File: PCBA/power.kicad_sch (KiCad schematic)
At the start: 8 parts, among them Q702 MMBT3904, U702 TC2014-3.3VxCTTR

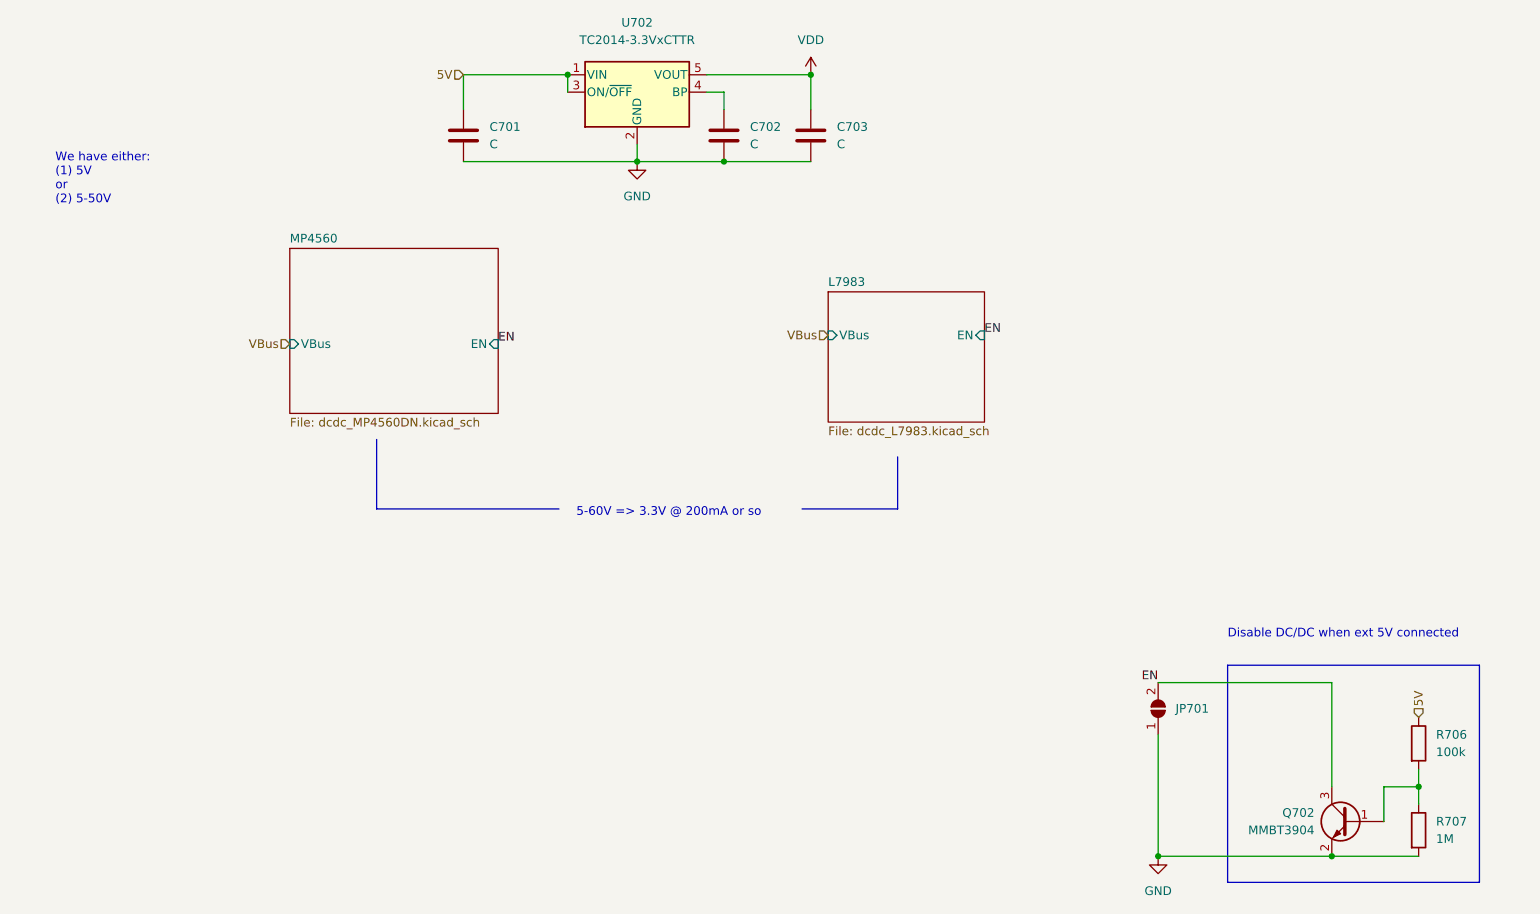
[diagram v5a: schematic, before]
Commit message: Step models for ports
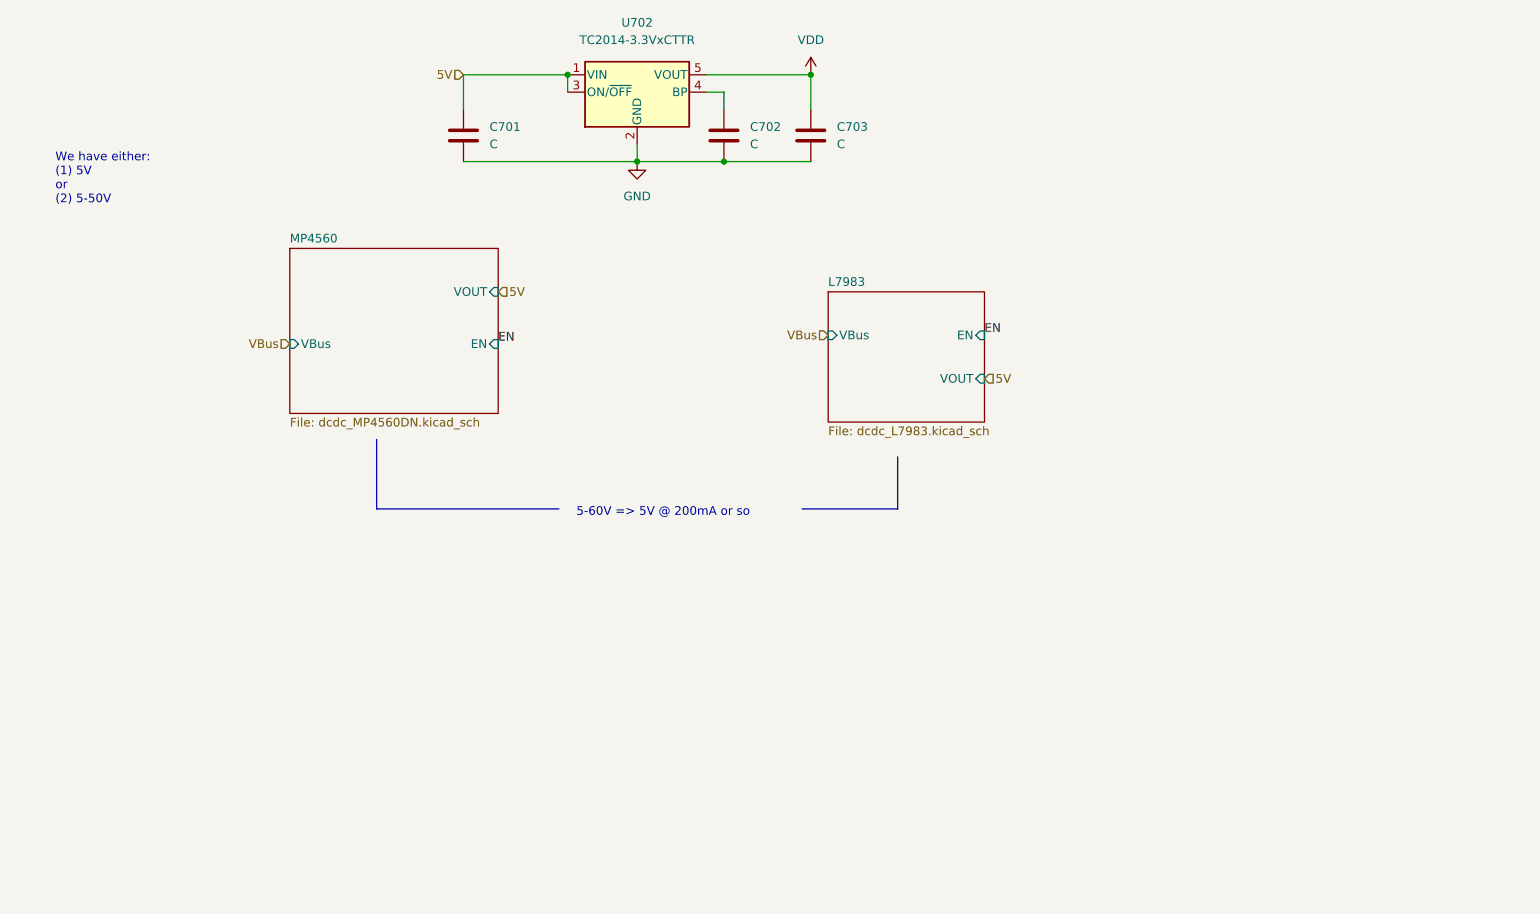
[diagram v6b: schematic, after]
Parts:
- removed JP701: Disable, Jumper:SolderJumper-2_P1.3mm_Open_Pad1.0x1.5mm, symbol Jumper:SolderJumper_2_Open
- removed Q702: MMBT3904, Package_TO_SOT_SMD:SOT-23, symbol Transistor_BJT:MMBT3904
- removed R706: 100k, Resistor_SMD:R_0603_1608Metric, symbol Device:R
- removed R707: 1M, Resistor_SMD:R_0603_1608Metric, symbol Device:R
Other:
- sheet L7983 ports: added VOUT; removed none
- sheet MP4560 ports: added VOUT; removed none
- note added: "5-60V => 5V @ 200mA or so"
- note removed: "5-60V => 3.3V @ 200mA or so"
- note removed: "Disable DC/DC when ext 5V connected"
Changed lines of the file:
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@@
 (kicad_sch (version 20211123) (generator eeschema)
   (paper "A4")
-  (junction (at 266.7 129.54) (diameter 0) (color 0 0 0 0)
-  )
-  (junction (at 228.6 139.7) (diameter 0) (color 0 0 0 0)
-  )
   (junction (at 142.24 25.4) (diameter 0) (color 0 0 0 0)
   )
   (junction (at 152.4 38.1) (diameter 0) (color 0 0 0 0)
   )
-  (junction (at 254 139.7) (diameter 0) (color 0 0 0 0)
-  )
   (junction (at 165.1 38.1) (diameter 0) (color 0 0 0 0)
   )
@@
     (stroke (width 0) (type default) (color 0 0 0 0))
   )
-  (wire (pts (xy 261.62 134.62) (xy 261.62 129.54))
-    (stroke (width 0) (type default) (color 0 0 0 0))
-  )
   (wire (pts (xy 165.1 27.94) (xy 165.1 30.48))
     (stroke (width 0) (type default) (color 0 0 0 0))
@@
     (stroke (width 0) (type default) (color 0 0 0 0))
   )
-  (polyline (pts (xy 238.76 111.76) (xy 275.59 111.76))
-    (stroke (width 0) (type default) (color 0 0 0 0))
-  )
-  (wire (pts (xy 266.7 127) (xy 266.7 129.54))
-    (stroke (width 0) (type default) (color 0 0 0 0))
-  )
   (wire (pts (xy 162.56 25.4) (xy 177.8 25.4))
     (stroke (width 0) (type default) (color 0 0 0 0))
   )
-  (wire (pts (xy 228.6 139.7) (xy 254 139.7))
-    (stroke (width 0) (type default) (color 0 0 0 0))
-  )
   (wire (pts (xy 162.56 27.94) (xy 165.1 27.94))
     (stroke (width 0) (type default) (color 0 0 0 0))
@@
     (stroke (width 0) (type default) (color 0 0 0 0))
   )
-  (wire (pts (xy 254 139.7) (xy 266.7 139.7))
-    (stroke (width 0) (type default) (color 0 0 0 0))
-  )
-  (wire (pts (xy 228.6 139.7) (xy 228.6 121.92))
-    (stroke (width 0) (type default) (color 0 0 0 0))
-  )
   (polyline (pts (xy 114.3 78.74) (xy 114.3 88.9))
     (stroke (width 0) (type default) (color 0 0 0 0))
   )
-  (polyline (pts (xy 275.59 143.51) (xy 275.59 111.76))
-    (stroke (width 0) (type default) (color 0 0 0 0))
-  )
   (polyline (pts (xy 190.5 81.28) (xy 190.5 88.9))
     (stroke (width 0) (type default) (color 0 0 0 0))
   )
-  (wire (pts (xy 254 114.3) (xy 254 129.54))
-    (stroke (width 0) (type default) (color 0 0 0 0))
-  )
   (wire (pts (xy 152.4 35.56) (xy 152.4 38.1))
     (stroke (width 0) (type default) (color 0 0 0 0))
   )
-  (wire (pts (xy 266.7 129.54) (xy 266.7 132.08))
-    (stroke (width 0) (type default) (color 0 0 0 0))
-  )
   (wire (pts (xy 177.8 25.4) (xy 177.8 30.48))
     (stroke (width 0) (type default) (color 0 0 0 0))
   )
-  (polyline (pts (xy 238.76 143.51) (xy 275.59 143.51))
-    (stroke (width 0) (type default) (color 0 0 0 0))
-  )
   (polyline (pts (xy 176.53 88.9) (xy 190.5 88.9))
     (stroke (width 0) (type default) (color 0 0 0 0))
@@
     (stroke (width 0) (type default) (color 0 0 0 0))
   )
-  (wire (pts (xy 228.6 114.3) (xy 254 114.3))
-    (stroke (width 0) (type default) (color 0 0 0 0))
-  )
   (wire (pts (xy 142.24 25.4) (xy 142.24 27.94))
     (stroke (width 0) (type default) (color 0 0 0 0))
   )
-  (polyline (pts (xy 238.76 111.76) (xy 238.76 143.51))
-    (stroke (width 0) (type default) (color 0 0 0 0))
-  )
-  (wire (pts (xy 261.62 129.54) (xy 266.7 129.54))
-    (stroke (width 0) (type default) (color 0 0 0 0))
-  )
   (wire (pts (xy 165.1 38.1) (xy 177.8 38.1))
     (stroke (width 0) (type default) (color 0 0 0 0))
   )
-  (text "Disable DC/DC when ext 5V connected" (at 238.76 107.95 0)
-    (effects (font (size 1.27 1.27)) (justify left bottom))
-  )
   (text "We have either:\n(1) 5V\nor\n(2) 5-50V" (at 67.31 44.45 0)
     (effects (font (size 1.27 1.27)) (justify left bottom))
   )
-  (text "5-60V => 3.3V @ 200mA or so" (at 143.51 90.17 0)
+  (text "5-60V => 5V @ 200mA or so" (at 143.51 90.17 0)
     (effects (font (size 1.27 1.27)) (justify left bottom))
   )
@@
   (label "EN" (at 203.2 63.5 0)
     (effects (font (size 1.27 1.27)) (justify left bottom))
-  )
-  (label "EN" (at 228.6 114.3 180)
-    (effects (font (size 1.27 1.27)) (justify right bottom))
   )
   (hierarchical_label "VBus" (shape input) (at 101.6 64.77 180)
     (effects (font (size 1.27 1.27)) (justify right))
   )
-  (hierarchical_label "5V" (shape input) (at 266.7 119.38 90)
+  (hierarchical_label "5V" (shape input) (at 203.2 69.85 0)
+    (effects (font (size 1.27 1.27)) (justify left))
+  )
+  (hierarchical_label "5V" (shape input) (at 132.08 57.15 0)
     (effects (font (size 1.27 1.27)) (justify left))
   )
@@
     (pin "5")
   )
-  (symbol (lib_id "Jumper:SolderJumper_2_Open") (at 228.6 118.11 90) (unit 1)
-    (in_bom yes) (on_board yes) (fields_autoplaced)
-    (property "Reference" "JP701" (id 0) (at 231.14 118.1099 90)
-      (effects (font (size 1.27 1.27)) (justify right))
-    )
-    (property "Value" "Disable" (id 1) (at 231.14 119.3799 90)
-      (effects (font (size 1.27 1.27)) (justify right) hide)
-    )
-    (property "Footprint" "Jumper:SolderJumper-2_P1.3mm_Open_Pad1.0x1.5mm" (id 2) (at 228.6 118.11 0)
-      (effects (font (size 1.27 1.27)) hide)
-    )
-    (property "Datasheet" "~" (id 3) (at 228.6 118.11 0)
-      (effects (font (size 1.27 1.27)) hide)
-    )
-    (pin "1")
-    (pin "2")
-  )
   (symbol (lib_id "Device:C") (at 165.1 34.29 0) (unit 1)
     (in_bom yes) (on_board yes) (fields_autoplaced)
@@
     (pin "2")
   )
-  (symbol (lib_id "Device:R") (at 266.7 123.19 0) (unit 1)
-    (in_bom yes) (on_board yes) (fields_autoplaced)
-    (property "Reference" "R706" (id 0) (at 269.24 121.9199 0)
-      (effects (font (size 1.27 1.27)) (justify left))
-    )
-    (property "Value" "100k" (id 1) (at 269.24 124.4599 0)
-      (effects (font (size 1.27 1.27)) (justify left))
-    )
-    (property "Footprint" "Resistor_SMD:R_0603_1608Metric" (id 2) (at 264.922 123.19 90)
-      (effects (font (size 1.27 1.27)) hide)
-    )
-    (property "Datasheet" "~" (id 3) (at 266.7 123.19 0)
-      (effects (font (size 1.27 1.27)) hide)
-    )
-    (pin "1")
-    (pin "2")
-  )
-  (symbol (lib_id "Device:R") (at 266.7 135.89 0) (unit 1)
-    (in_bom yes) (on_board yes) (fields_autoplaced)
-    (property "Reference" "R707" (id 0) (at 269.24 134.6199 0)
-      (effects (font (size 1.27 1.27)) (justify left))
-    )
-    (property "Value" "1M" (id 1) (at 269.24 137.1599 0)
-      (effects (font (size 1.27 1.27)) (justify left))
-    )
-    (property "Footprint" "Resistor_SMD:R_0603_1608Metric" (id 2) (at 264.922 135.89 90)
-      (effects (font (size 1.27 1.27)) hide)
-    )
-    (property "Datasheet" "~" (id 3) (at 266.7 135.89 0)
-      (effects (font (size 1.27 1.27)) hide)
-    )
-    (pin "1")
-    (pin "2")
-  )
   (symbol (lib_id "Device:C") (at 177.8 34.29 0) (unit 1)
     (in_bom yes) (on_board yes) (fields_autoplaced)
@@
     (pin "2")
   )
-  (symbol (lib_id "power:GND") (at 228.6 139.7 0) (unit 1)
-    (in_bom yes) (on_board yes) (fields_autoplaced)
-    (property "Reference" "#PWR0154" (id 0) (at 228.6 146.05 0)
-      (effects (font (size 1.27 1.27)) hide)
-    )
-    (property "Value" "GND" (id 1) (at 228.6 144.78 0))
-    (property "Footprint" "" (id 2) (at 228.6 139.7 0)
-      (effects (font (size 1.27 1.27)) hide)
-    )
-    (property "Datasheet" "" (id 3) (at 228.6 139.7 0)
-      (effects (font (size 1.27 1.27)) hide)
-    )
-    (pin "1")
-  )
   (symbol (lib_id "Device:C") (at 127 34.29 0) (unit 1)
     (in_bom yes) (on_board yes) (fields_autoplaced)
@@
     (pin "1")
     (pin "2")
-  )
-  (symbol (lib_id "Transistor_BJT:MMBT3904") (at 256.54 134.62 0) (mirror y) (unit 1)
-    (in_bom yes) (on_board yes) (fields_autoplaced)
-    (property "Reference" "Q702" (id 0) (at 251.46 133.3499 0)
-      (effects (font (size 1.27 1.27)) (justify left))
-    )
-    (property "Value" "MMBT3904" (id 1) (at 251.46 135.8899 0)
-      (effects (font (size 1.27 1.27)) (justify left))
-    )
-    (property "Footprint" "Package_TO_SOT_SMD:SOT-23" (id 2) (at 251.46 136.525 0)
-      (effects (font (size 1.27 1.27) italic) (justify left) hide)
-    )
-    (property "Datasheet" "https://www.onsemi.com/pub/Collateral/2N3903-D.PDF" (id 3) (at 256.54 134.62 0)
-      (effects (font (size 1.27 1.27)) (justify left) hide)
-    )
-    (pin "1")
-    (pin "2")
-    (pin "3")
   )
   (symbol (lib_id "power:VDD") (at 177.8 25.4 0) (unit 1)
@@
       (effects (font (size 1.27 1.27)) (justify right))
     )
+    (pin "VOUT" input (at 203.2 69.85 0)
+      (effects (font (size 1.27 1.27)) (justify right))
+    )
   )
   (sheet (at 101.6 50.8) (size 30.48 24.13) (fields_autoplaced)
@@
       (effects (font (size 1.27 1.27)) (justify left))
     )
-  )
+    (pin "VOUT" input (at 132.08 57.15 0)
+      (effects (font (size 1.27 1.27)) (justify right))
+    )
+  )
